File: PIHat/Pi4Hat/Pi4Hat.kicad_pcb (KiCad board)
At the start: 2 copper layers, 65 x 56 mm, 18 parts, among them J1 GPIO, J2 U.FL-R-SMT-1_80_, J3 U.FL-R-SMT-1_80_, J4 U.FL-R-SMT-1_80_, J5 1725672, J6 1725672, J7 Conn_01x03_Socket, J8 GPIO

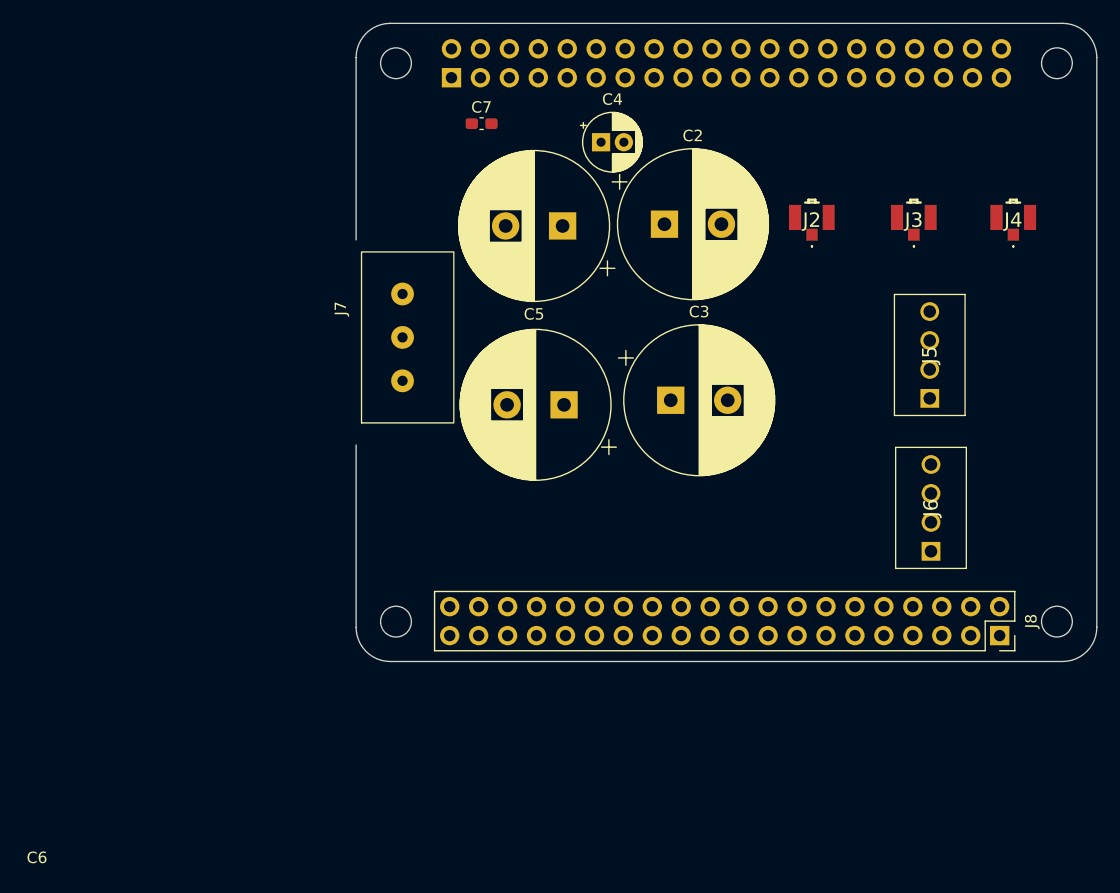
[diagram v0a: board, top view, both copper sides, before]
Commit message: added new rpi power board
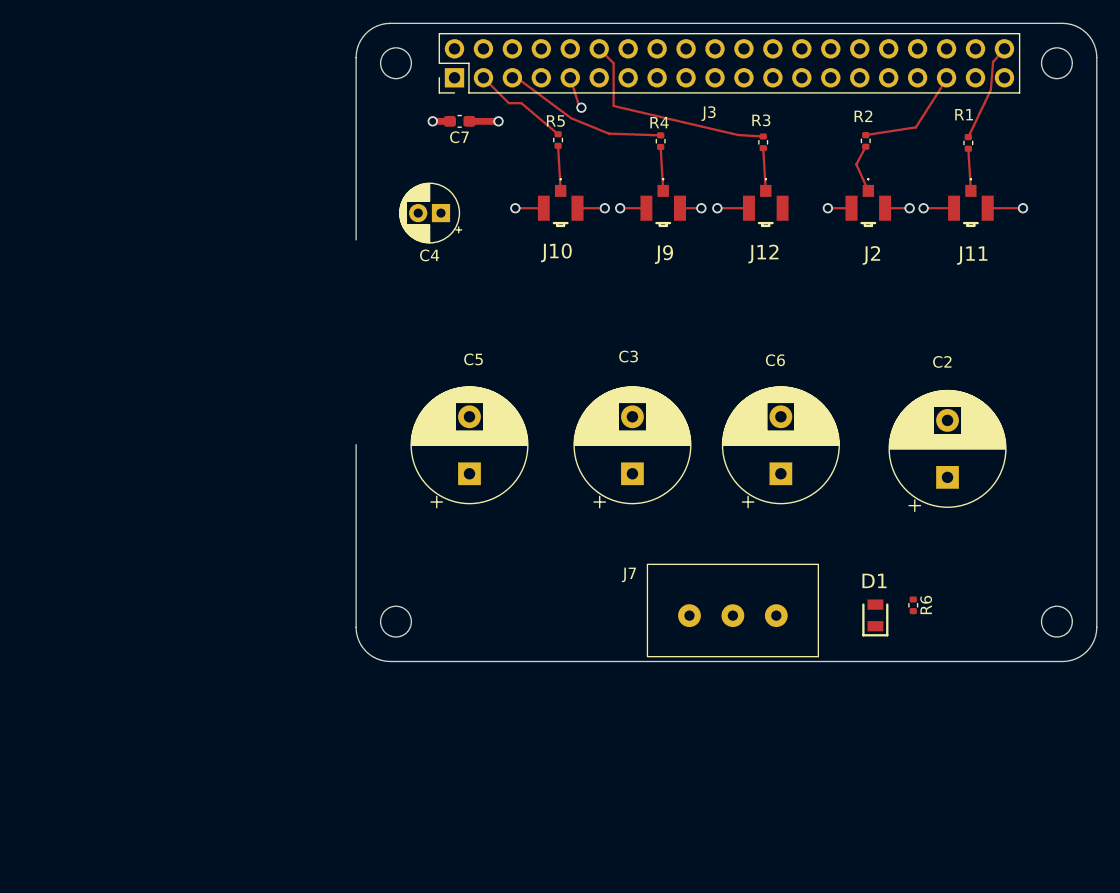
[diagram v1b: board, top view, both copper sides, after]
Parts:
- removed J1, J8: GPIO, Connector_PinSocket_2.54mm:PinSocket_2x20_P2.54mm_Vertical
- removed J4: U.FL-R-SMT-1_80_, samsys:UFLRSMT180
- removed J5, J6: 1725672, samsys:1725672
- added D1: LS_R976, samsys:LEDC2012X40N, F.Cu at (145.6, 96.0)
- added J10: U.FL-R-SMT-1_80_, samsys:UFLRSMT180, F.Cu at (118.0, 60.2)
- added J11: U.FL-R-SMT-1_80_, samsys:UFLRSMT180, F.Cu at (153.9, 60.2)
- added J12: U.FL-R-SMT-1_80_, samsys:UFLRSMT180, F.Cu at (135.9, 60.2)
- added J9: U.FL-R-SMT-1_80_, samsys:UFLRSMT180, F.Cu at (127.0, 60.2)
- added R1: 22, Resistor_SMD:R_0402_1005Metric, F.Cu at (153.7, 54.5)
- added R2: 22, Resistor_SMD:R_0402_1005Metric, F.Cu at (144.7, 54.3)
- added R3: 22, Resistor_SMD:R_0402_1005Metric, F.Cu at (135.7, 54.4)
- added R4: 22, Resistor_SMD:R_0402_1005Metric, F.Cu at (126.7, 54.3)
- added R5: 22, Resistor_SMD:R_0402_1005Metric, F.Cu at (117.7, 54.2)
- added R6: 1k, Resistor_SMD:R_0402_1005Metric, F.Cu at (148.9, 95.1)
- C2, C3, C5, C6: footprint Capacitor_THT:CP_Radial_D13.0mm_P5.00mm -> Capacitor_THT:CP_Radial_D10.0mm_P5.00mm
- J3: value U.FL-R-SMT-1_80_ -> 70246-4001; footprint samsys:UFLRSMT180 -> Connector_PinHeader_2.54mm:PinHeader_2x20_P2.54mm_Vertical
- moved J3 42.1 mm to (108.6, 48.8), turned to 90 degrees
- moved J7 37.9 mm to (133.1, 96.0), turned to 180 degrees
- moved C2 33.3 mm to (151.9, 83.8), turned to 90 degrees
- moved C5 23.2 mm to (110.0, 83.5), turned to 90 degrees
- moved C6 20.0 mm to (137.3, 83.5), turned to 90 degrees
- moved C4 15.4 mm to (107.5, 60.6), turned to 180 degrees
- moved C3 7.27 mm to (124.2, 83.5), turned to 90 degrees
- moved J2 5.01 mm to (144.9, 60.2), turned to 180 degrees
- moved C7 1.94 mm to (109.1, 52.6), turned to 180 degrees
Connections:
- J2 pad 1: /GPIO26 -> Net-(J2-SIG)
- J3 pad 1: /GPIO18/PCM.CLK -> +3.3V
- J3 pad 2: GND -> +5V
- J3 pad 3: GND -> /GPIO2/SDA1
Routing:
- net GND: track 0.00 -> 26.2 mm, vias 0 -> 11
- net /GPIO18/I2S BCL: track 0.00 -> 19.0 mm
- net /GPIO3/SCL1: track 0.00 -> 14.3 mm
- net +5V: track 0.00 -> 12.2 mm, vias 0 -> 1
- net /GPIO19/I2S LRCK: track 0.00 -> 9.79 mm
- net /GPIO21/I2S DOUT: track 0.00 -> 8.81 mm
- net /GPIO2/SDA1: track 0.00 -> 8.47 mm
- net Net-(J2-SIG): track 0.00 -> 4.31 mm
- net Net-(J10-SIG): track 0.00 -> 3.96 mm
- net Net-(J9-SIG): track 0.00 -> 3.86 mm
- net Net-(J12-SIG): track 0.00 -> 3.76 mm
- net Net-(J11-SIG): track 0.00 -> 3.71 mm
- added copper zone on In2.Cu, net +5V
- added copper zone on In1.Cu, net GND
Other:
- copper layers 2 -> 4
